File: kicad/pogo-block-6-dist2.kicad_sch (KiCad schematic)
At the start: 62 parts, among them U32 CD4053, U36 TL072, U37 TL072, U42 TL072, U43 TL072, U76 CD4053

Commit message: 0018: block-6 stage 2 - distortion BEFORE bandpass (0017 reorder)
The core 0017 change: flip the per-band order from SVF->DIST to DIST->SVF to
match the plugin (Pogo.cpp:443-451). Realized as a net re-point across the 7
split sections (no part changes):
  LP1_OUT / BP3IN  ->  distN (R18/R20/R22 distortion inputs)
                   ->  mux out (BPn_DISTOUT)  ->  svfN SUM_AMP (R13)
                   ->  SVF v1 buffer (BPn_BANDOUT / BP3_TAP)  ->  mix wet summer
- BP1/BP2 take the LP1 band; BP3 takes BP3IN (the ALT/LP1 selector, stage 3).
- BP3 OUT tap now taken post-bandpass (BP3_TAP = svf3 v1), matching the plugin
  (prevOut[2]); block-B keeps the BP3_TAP net name (no block-B change).
- spec §1/§2 updated: signal order, DIST knob, ALT path (through-VCA/BP3-only),
  BP3 tap point.

Boundary symmetry verified for all re-pointed nets; all 5 --check gates +
parity green.

https://claude.ai/code/session_013jFXG5oeMVSYP7iRpwGvtQ
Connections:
- net BP2_BPBUF_L renamed LP1_OUT_L
- net BP2_BPBUF_R renamed LP1_OUT_R
- net BP2_DIST_L renamed BP2_DISTOUT_L
- net BP2_DIST_R renamed BP2_DISTOUT_R
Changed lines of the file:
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@@
   (effects (font (size 1.016 1.016)) (justify left))
 )
-(global_label "BP2_BPBUF_L"
+(global_label "LP1_OUT_L"
   (shape output)
   (at 40.000 373.810 0)
   (effects (font (size 1.016 1.016)) (justify left))
 )
-(global_label "BP2_BPBUF_L"
+(global_label "LP1_OUT_L"
   (shape output)
   (at 160.000 373.810 0)
   (effects (font (size 1.016 1.016)) (justify left))
 )
-(global_label "BP2_BPBUF_L"
+(global_label "LP1_OUT_L"
   (shape output)
   (at 100.000 428.810 0)
   (effects (font (size 1.016 1.016)) (justify left))
 )
-(global_label "BP2_BPBUF_L"
+(global_label "LP1_OUT_L"
   (shape output)
   (at 40.000 538.810 0)
   (effects (font (size 1.016 1.016)) (justify left))
 )
-(global_label "BP2_BPBUF_L"
+(global_label "LP1_OUT_L"
   (shape output)
   (at 100.000 538.810 0)
   (effects (font (size 1.016 1.016)) (justify left))
 )
-(global_label "BP2_BPBUF_R"
+(global_label "LP1_OUT_R"
   (shape output)
   (at 40.000 758.810 0)
   (effects (font (size 1.016 1.016)) (justify left))
 )
-(global_label "BP2_BPBUF_R"
+(global_label "LP1_OUT_R"
   (shape output)
   (at 160.000 758.810 0)
   (effects (font (size 1.016 1.016)) (justify left))
 )
-(global_label "BP2_BPBUF_R"
+(global_label "LP1_OUT_R"
   (shape output)
   (at 100.000 813.810 0)
   (effects (font (size 1.016 1.016)) (justify left))
 )
-(global_label "BP2_BPBUF_R"
+(global_label "LP1_OUT_R"
   (shape output)
   (at 40.000 923.810 0)
   (effects (font (size 1.016 1.016)) (justify left))
 )
-(global_label "BP2_BPBUF_R"
+(global_label "LP1_OUT_R"
   (shape output)
   (at 100.000 923.810 0)
@@
   (effects (font (size 1.016 1.016)) (justify left))
 )
-(global_label "BP2_DIST_L"
+(global_label "BP2_DISTOUT_L"
   (shape output)
   (at 48.890 50.160 0)
   (effects (font (size 1.016 1.016)) (justify left))
 )
-(global_label "BP2_DIST_R"
+(global_label "BP2_DISTOUT_R"
   (shape output)
   (at 48.890 42.540 0)

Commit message: 0018: block-6 stage 5 - variable DRIVE (THAT2180 VCA per band)
Build the per-band variable-drive stage the plugin needs (driveCv into the
waveshaper). A stereo THAT2180 current-in/I-V-out VCA per band, inserted at the
distortion input, mirroring the proven block-4 cell pin-for-pin:
  band -> R_in(20k) -> THAT2180.1 ; .8 -> TL074 I/V(-) + R_f(20k) -> BPn_DRIVEOUT
  -> SC/HC/WF cells.  Ec+ (pin2) via Bourns unity trim <- V_DRIVE_CTRL.
Drive control: per-band DRIVE knob (RV33/36/39) + DRIVE CV (MOD_BPn_DIST from
block-3) summed (TL074 half) into Ec+; knob=0.20 ~= unity. A single dB-law VGA
per band approximates the plugin's per-mode gain (SC exp vs HC/WF linear) -- a
documented deviation; exact knob->Ec+ dB law + unity bias are Phase-3R (like
block-4's Ec+ scaling).

Parts: +6 THAT2180 (U85-90), +3 TL074 (U91-93 I/V+summer), +6 Ec+ trims
(RV51-56), R153-176, decoupling. New boundary MOD_BPn_DIST; BPn_DRIVEOUT
internal. RV33/36/39 reused.

NOTE: the I/V stage inverts (as in block-4) -> one inversion added to the BP
wet path; reconcile in the S7 mix polarity-restore so wet sums with dry.

(An initial LM13700-OTA-VGA attempt was rolled back: its input wasn't scaled to
the OTA linear range -- would saturate on +-5V audio. Rebuilt on THAT2180 per
user.) All 5 --check gates + parity green; wiring reviewed vs block-4 template.

https://claude.ai/code/session_013jFXG5oeMVSYP7iRpwGvtQ
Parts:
- added C110_U87n, C110_U87p, C110_U88n, C110_U88p, C110_U92n, C110_U92p: 100nF, symbol Device:C
- added R161, R162, R163, R164: 20k, symbol Device:R
- added R165, R166, R167, R168: 100k, symbol Device:R
- added RV36: BP2_DIST, POGO_Potentiometer_THT:Potentiometer_Alpha_RD901F-40-00D_Single_Vertical_CircularHoles, symbol Device:R_POT
- added RV53: BP2_DRIVE_UNITY_L, POGO_Potentiometer_SMD:Potentiometer_Bourns_3224W, symbol Device:R_POT
- added RV54: BP2_DRIVE_UNITY_R, POGO_Potentiometer_SMD:Potentiometer_Bourns_3224W, symbol Device:R_POT
- added U87, U88: THAT2180, POGO_Package_SIP:SIP-8_2.54mm, symbol POGO:THAT2180
- added U92: TL074, symbol Amplifier_Operational:TL074
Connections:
- net +12V: now also C110_U87p.2, C110_U88p.2, C110_U92p.2, U87.5 (V-), U88.5 (V-), U92.11 (V-)
- net -12V: now also C110_U87n.2, C110_U88n.2, C110_U92n.2, U87.7 (V+), U88.7 (V+), U92.4 (V+)
- net GND: now also C110_U87n.1, C110_U87p.1, C110_U88n.1, C110_U88p.1, C110_U92n.1, C110_U92p.1, RV36.3, U87.1 (Input), U87.2 (Ec+), U87.3 (Ec-), U88.1 (Input), U88.2 (Ec+), U88.3 (Ec-), U92.13 (In-), U92.2 (In-), U92.6 (In-), U92.9 (In-)
- net LP1_OUT_L: now also R161.2; no longer C_WF_2La.2, C_WF_2Lb.2, R18_2L.2, R20_2L.2, R22_2L.2
- net LP1_OUT_R: now also R162.2; no longer C_WF_2Ra.2, C_WF_2Rb.2, R18_2R.2, R20_2R.2, R22_2R.2
- net V5LOGIC: now also R167.2, RV36.1
- new net BP2_DRIVEIN_L: R161.1, U87.6 (Gnd)
- new net BP2_DRIVEIN_R: R162.1, U88.6 (Gnd)
- new net BP2_DRIVEIV_L: R163.2, U92.3 (In+)
- new net BP2_DRIVEIV_R: R164.2, U92.5 (In+)
- new net BP2_DRIVEOUT_L: C_WF_2La.2, C_WF_2Lb.2, R163.1, R18_2L.2, R20_2L.2, R22_2L.2, U92.1 (Out)
- new net BP2_DRIVEOUT_R: C_WF_2Ra.2, C_WF_2Rb.2, R164.1, R18_2R.2, R20_2R.2, R22_2R.2, U92.7 (Out)
- new net BP2_DRIVE_KNOB: R165.2, RV36.2 (Wiper)
- new net BP2_DRIVE_SPARE: U92.12 (In+), U92.14 (Out)
- new net BP2_DRIVE_SUM: R165.1, R166.1, R167.1, R168.2, U92.10 (In+)
- new net EC_BP2_DRIVE_L: RV53.2 (Wiper), RV53.3, U87.4 (Sym)
- new net EC_BP2_DRIVE_R: RV54.2 (Wiper), RV54.3, U88.4 (Sym)
- new net MOD_BP2_DIST: R166.2
- new net V_DRIVE_CTRL_2: R168.1, RV53.1, RV54.1, U92.8 (Out)

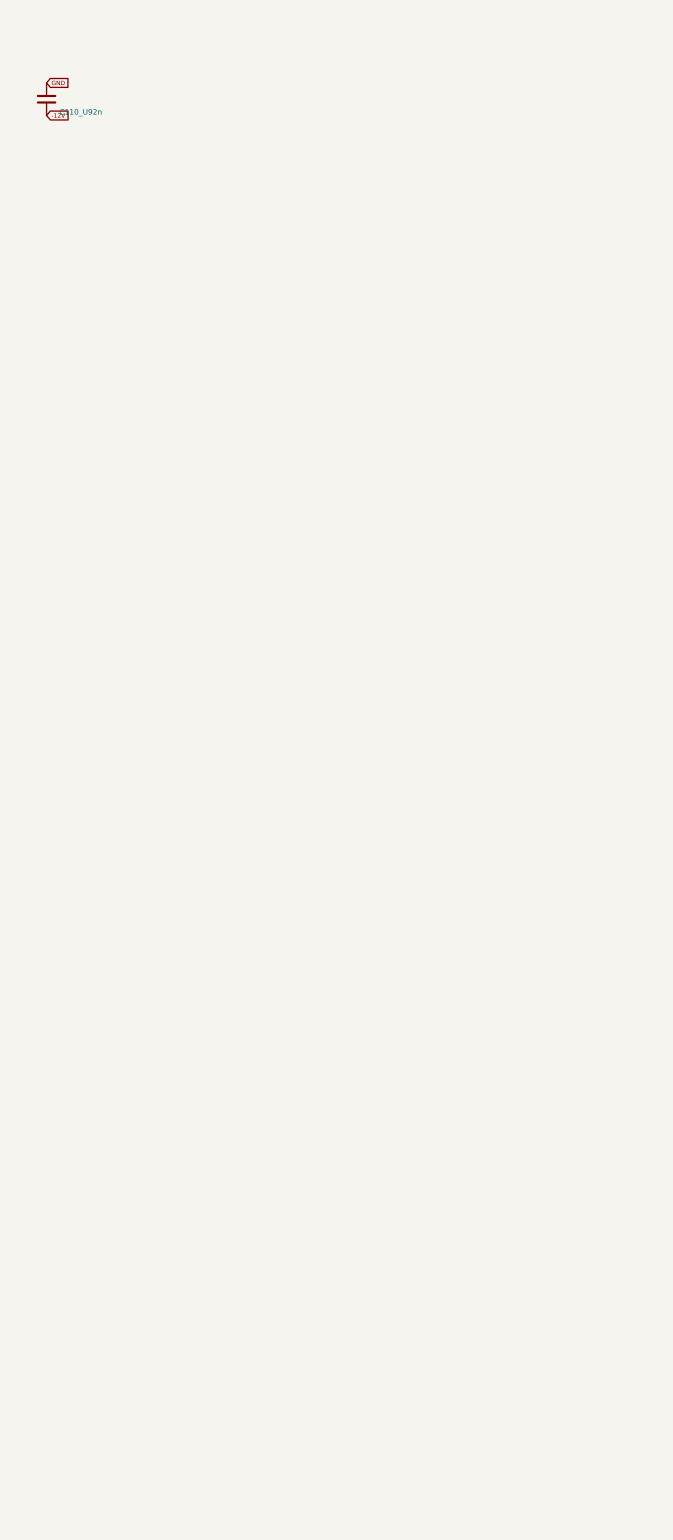
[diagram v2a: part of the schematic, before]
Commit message: 0018: block-6 stage 6 - per-band CLIP LED drivers
The plugin lights BPn_CLIP when max(|distOut_L|,|distOut_R|) > 4V; the panel
has the CLIP LEDs but no hardware drove them. Build a per-band window
detector on the distortion output (BPn_DISTOUT_L/R, the CD4053 mux output):
- TL074 (U94/U95/U96) as 4 comparators per band: DISTOUT_L>+4, <-4,
  DISTOUT_R>+4, <-4, with ~2.2M hysteresis. Outputs diode-OR (D14_*) into
  the panel CLIP LED via a current-limit R.
- Shared +/-4V threshold from a 20k/10k divider off +/-12 (dist1), exported
  as VREF_P4/VREF_N4 boundary nets to dist2/dist3.
- CLIP LED component rows added for BP1/2/3.

All 5 --check gates + parity green. Exact threshold trim is Phase-3R.

https://claude.ai/code/session_013jFXG5oeMVSYP7iRpwGvtQ
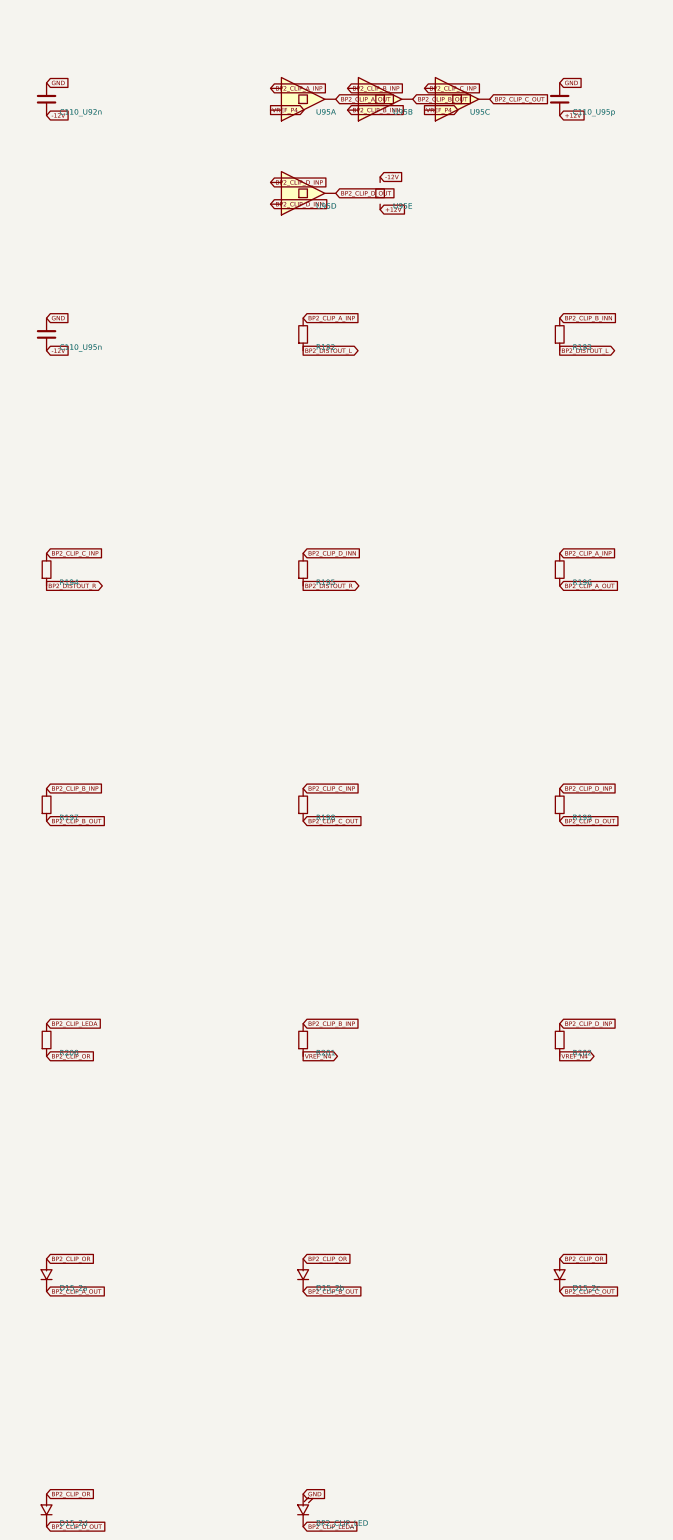
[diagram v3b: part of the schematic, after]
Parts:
- added BP2_CLIP_LED: BP2_CLIP, POGO_LED_THT:LED_D3.0mm, symbol Device:LED
- added C110_U95n, C110_U95p: 100nF, symbol Device:C
- added D15_2a, D15_2b, D15_2c, D15_2d: 1N4148W, POGO_Diode_SMD:D_SOD-123, symbol Device:D
- added R192, R193, R194, R195, R201, R202: 100k, symbol Device:R
- added R196, R197, R198, R199: 2.2M, symbol Device:R
- added R200: 1k, symbol Device:R
- added U95: TL074, symbol Amplifier_Operational:TL074
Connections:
- net +12V: now also C110_U95p.2, U95.11 (V-)
- net -12V: now also C110_U95n.2, U95.4 (V+)
- net BP2_DISTOUT_L: now also R192.2, R193.2
- net BP2_DISTOUT_R: now also R194.2, R195.2
- net GND: now also BP2_CLIP_LED.A, C110_U95n.1, C110_U95p.1
- new net BP2_CLIP_A_INP: R192.1, R196.1, U95.2 (In-)
- new net BP2_CLIP_A_OUT: D15_2a.K, R196.2, U95.1 (Out)
- new net BP2_CLIP_B_INN: R193.1, U95.5 (In+)
- new net BP2_CLIP_B_INP: R197.1, R201.1, U95.6 (In-)
- new net BP2_CLIP_B_OUT: D15_2b.K, R197.2, U95.7 (Out)
- new net BP2_CLIP_C_INP: R194.1, R198.1, U95.9 (In-)
- new net BP2_CLIP_C_OUT: D15_2c.K, R198.2, U95.8 (Out)
- new net BP2_CLIP_D_INN: R195.1, U95.12 (In+)
- new net BP2_CLIP_D_INP: R199.1, R202.1, U95.13 (In-)
- new net BP2_CLIP_D_OUT: D15_2d.K, R199.2, U95.14 (Out)
- new net BP2_CLIP_LEDA: BP2_CLIP_LED.K, R200.1
- new net BP2_CLIP_OR: D15_2a.A, D15_2b.A, D15_2c.A, D15_2d.A, R200.2
- new net VREF_N4: R201.2, R202.2
- new net VREF_P4: U95.10 (In+), U95.3 (In+)

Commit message: 0020 HIGH-3: VCA Ec+ injection trims + V_CTRL buffer (10 cells, last cluster)
Replaced the useless series-rheostat-into-high-Z-Ec+ unity trims (~0.004dB
authority) with SPICE-validated voltage-injection trims across all 10 VCA cells:
- block-4 (4 cells: main L/R + ALT L/R): +U97 TL072 buffers the unbuffered AMT
  wiper -> V_CTRL_BUF -> 4x R_ec(10k) -> Ec+ (decouples the cells). Trims RV1/2/46/47
  500ohm->10k as dividers across a shared ±1.2V ref (R233/R234), wiper->R_inj(1M)->Ec+.
- block-6 dist1/2/3 (6 DRIVE cells): same injection trim; V_DRIVE_CTRL_n is already
  an op-amp output (low-Z) so no extra buffer - just per-section ±ref divider + R_ec/R_inj.
  RV51-56 500ohm->10k.
SPICE vca_ecplus_full.cir: g_ctrl 0.984, ±2dB unity authority, nulls bias offset.
New: U97, R233-R260, C117/C118; ~30 parts. All --check gates + JS/Py parity green,
0 schematic FAIL. (Absolute 6.1mV/dB is [NV], absorbed by the ±2dB trim.)

https://claude.ai/code/session_013jFXG5oeMVSYP7iRpwGvtQ
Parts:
- added BP2_CLIP_LED: BP2_CLIP, POGO_LED_THT:LED_D3.0mm, symbol Device:LED
- added D15_2a, D15_2b, D15_2c, D15_2d: 1N4148W, POGO_Diode_SMD:D_SOD-123, symbol Device:D
- added R202: 100k, symbol Device:R
- C110_U87n, C110_U88n, C110_U88p, C110_U92p: renamed from U95; value TL074 -> 100nF; symbol Amplifier_Operational:TL074 -> Device:C
- C110_U87p: renamed from U95; value TL074 -> 100nF; footprint POGO_Package_SO:SOIC-14_3.9x8.7mm_P1.27mm -> (none); symbol Amplifier_Operational:TL074 -> Device:C
- C110_U95n: renamed from R197; value 2.2M -> 100nF; symbol Device:R -> Device:C
- C110_U95p: renamed from R196; value 2.2M -> 100nF; symbol Device:R -> Device:C
- R192: renamed from R198; value 2.2M -> 100k
- R193: renamed from R199; value 2.2M -> 100k
- R194: renamed from R200; value 1k -> 100k
- R196: renamed from R202; value 100k -> 2.2M
- R197: renamed from D15_2a; value 1N4148W -> 2.2M; footprint POGO_Diode_SMD:D_SOD-123 -> (none); symbol Device:D -> Device:R
- R198: renamed from D15_2b; value 1N4148W -> 2.2M; footprint POGO_Diode_SMD:D_SOD-123 -> (none); symbol Device:D -> Device:R
- R199: renamed from D15_2c; value 1N4148W -> 2.2M; footprint POGO_Diode_SMD:D_SOD-123 -> (none); symbol Device:D -> Device:R
- R200: renamed from D15_2d; value 1N4148W -> 1k; footprint POGO_Diode_SMD:D_SOD-123 -> (none); symbol Device:D -> Device:R
- R201: renamed from BP2_CLIP_LED; value BP2_CLIP -> 100k; footprint POGO_LED_THT:LED_D3.0mm -> (none); symbol Device:LED -> Device:R
- R249: renamed from RV36; value BP2_DIST -> 45k3; footprint POGO_Potentiometer_THT:Potentiometer_Alpha_RD901F-40-00D_Single_Vertical_CircularHoles -> (none); symbol Device:R_POT -> Device:R
- R250: renamed from C110_U87p; value 100nF -> 45k3; symbol Device:C -> Device:R
- R251: renamed from C110_U87n; value 100nF -> 10k; symbol Device:C -> Device:R
- R252: renamed from C110_U88p; value 100nF -> 10k; symbol Device:C -> Device:R
- R253: renamed from C110_U88n; value 100nF -> 1M; symbol Device:C -> Device:R
- R254: renamed from C110_U92p; value 100nF -> 1M; symbol Device:C -> Device:R
- RV36: renamed from C110_U92n; value 100nF -> BP2_DIST; footprint (none) -> POGO_Potentiometer_THT:Potentiometer_Alpha_RD901F-40-00D_Single_Vertical_CircularHoles; symbol Device:C -> Device:R_POT
- U95: renamed from R194; value 100k -> TL074; symbol Device:R -> Amplifier_Operational:TL074
- U95: renamed from R193; value 100k -> TL074; symbol Device:R -> Amplifier_Operational:TL074
- U95: renamed from C110_U95n; value 100nF -> TL074; footprint (none) -> POGO_Package_SO:SOIC-14_3.9x8.7mm_P1.27mm; symbol Device:C -> Amplifier_Operational:TL074
- U95: renamed from R195; value 100k -> TL074; symbol Device:R -> Amplifier_Operational:TL074
- U95: renamed from R192; value 100k -> TL074; symbol Device:R -> Amplifier_Operational:TL074
- renumbered C110_U95p to C110_U92n, R201 to R195
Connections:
- net +12V: now also C110_U87p.2, C110_U88p.2, C110_U92p.2, C110_U95p.2, R249.2, U95.11 (V-); no longer C110_U92n.2, C110_U92p.11 (V-), R250.2, R252.2, R254.2
- net -12V: now also C110_U87n.2, C110_U88n.2, C110_U92n.2, C110_U95n.2, R250.2, U95.4 (V+); no longer C110_U92p.4 (V+), R251.2, R253.2, RV36.2, U95.2
- net BP2_CLIP_A_INP: now also R192.1, R196.1, U95.2 (In-); no longer C110_U87p.2 (In-), C110_U95p.1, U95.1
- net BP2_CLIP_A_OUT: now also R196.2, U95.1 (Out), D15_2a.K; no longer C110_U87p.1 (Out), C110_U95p.2, R197.K
- net BP2_CLIP_B_INN: now also R193.1, U95.5 (In+); no longer C110_U87n.5 (In+), U95.1
- net BP2_CLIP_B_INP: now also R197.1, R201.1, U95.6 (In-); no longer C110_U87n.6 (In-), C110_U95n.1, R195.1
- net BP2_CLIP_B_OUT: now also R197.2, U95.7 (Out), D15_2b.K; no longer C110_U87n.7 (Out), C110_U95n.2, R198.K
- net BP2_CLIP_C_INP: now also R194.1, R198.1, U95.9 (In-); no longer C110_U88p.9 (In-), R192.1, U95.1
- net BP2_CLIP_C_OUT: now also R198.2, U95.8 (Out), D15_2c.K; no longer C110_U88p.8 (Out), R192.2, R199.K
- net BP2_CLIP_D_INN: now also R195.1, U95.12 (In+); no longer C110_U88n.12 (In+), U95.1
- net BP2_CLIP_D_INP: now also R199.1, U95.13 (In-), R202.1; no longer C110_U88n.13 (In-), R193.1, R196.1
- net BP2_CLIP_D_OUT: now also R199.2, U95.14 (Out), D15_2d.K; no longer C110_U88n.14 (Out), R193.2, R200.K
- net BP2_CLIP_LEDA: now also R200.1, BP2_CLIP_LED.K; no longer R194.1, R201.K
- net BP2_CLIP_OR: now also R200.2, D15_2a.A, D15_2b.A, D15_2c.A, D15_2d.A; no longer R194.2, R197.A, R198.A, R199.A, R200.A
- net BP2_DISTOUT_L: now also R192.2, R193.2; no longer U95.2, U95.2
- net BP2_DISTOUT_R: now also R194.2, R195.2; no longer U95.2, U95.2
- net BP2_DRIVE_KNOB: now also RV36.2 (Wiper); no longer R249.2 (Wiper)
- net EC_BP2_DRIVE_L: now also R251.1, R253.1; no longer RV53.2 (Wiper), RV53.3
- net EC_BP2_DRIVE_R: now also R252.1, R254.1; no longer RV54.2 (Wiper), RV54.3
- net GND: now also C110_U87n.1, C110_U87p.1, C110_U88n.1, C110_U88p.1, C110_U92p.1, C110_U95n.1, C110_U95p.1, RV36.3, BP2_CLIP_LED.A; no longer R201.A, R249.3, R250.1, R251.1, R252.1, R253.1, R254.1, RV36.1, U95.1
- net V5LOGIC: now also RV36.1; no longer R249.1
- net VREF_N4: now also R201.2, R202.2; no longer R195.2, R196.2
- net VREF_P4: now also U95.10 (In+), U95.3 (In+); no longer C110_U87p.3 (In+), C110_U88p.10 (In+)
- net V_DRIVE_CTRL_2: now also R251.2, R252.2; no longer RV53.1, RV54.1
- new net REF_N2: R250.1, RV53.1, RV54.1
- new net REF_P2: R249.1, RV53.3, RV54.3
- new net TRIMW_BP2_L: R253.2, RV53.2 (Wiper)
- new net TRIMW_BP2_R: R254.2, RV54.2 (Wiper)
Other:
- moved on the sheet: C110_U92n, U95E

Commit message: 0025: FIX the HIGH-3 ref-divider bug the SPICE-math gate found (block-4 + block-6)
ref_divider.cir derived REF_P from the actual netlist and got +-0.32V, not the
+-1.2V spec.md:166 + the 0020 HIGH-3 design claimed. Root cause (my error in
0020): R233/R234 sized 45.3k assuming a SINGLE 10k bridge, but all 4 unity trims
(RV1/RV2/RV46/RV47) load REF_P<->REF_N in PARALLEL = 2.5k -> REF_P collapses to
0.32V -> Ec+ injection authority was ~+-0.5dB, not the intended +-2dB. block-6
DRIVE refs had the same bug (2 pots = 5k bridge).

FIX:
- block-4: R233/R234 45k3->11k3 (-> +1.195V at the 2.5k load).
- block-6 dist1/2/3: R243/244/249/250/255/256 45k3->22k6 (-> +1.2V at the 5k load).
- ref_divider deck now pins +1.195V + binds R233=11k3, so a regression to 45k3
  FAILS the gate. Regenerated block-4/dist1/2/3 schematics + BOM.

All 7 --check gates green (incl. SPICE). Second real design error the SPICE-math
methodology has found; first to correct live netlist component values.

https://claude.ai/code/session_013jFXG5oeMVSYP7iRpwGvtQ
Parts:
- R249, R250: value 45k3 -> 22k6
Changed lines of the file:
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@@
   (property "Reference" "R249" (at 43.000 1418.000 0)
     (effects (font (size 1.27 1.27)) (justify left)))
-  (property "Value" "45k3" (at 43.000 1414.500 0)
+  (property "Value" "22k6" (at 43.000 1414.500 0)
     (effects (font (size 1.016 1.016)) (justify left) (hide yes)))
 )
@@
   (property "Reference" "R250" (at 103.000 1418.000 0)
     (effects (font (size 1.27 1.27)) (justify left)))
-  (property "Value" "45k3" (at 103.000 1414.500 0)
+  (property "Value" "22k6" (at 103.000 1414.500 0)
     (effects (font (size 1.016 1.016)) (justify left) (hide yes)))
 )
